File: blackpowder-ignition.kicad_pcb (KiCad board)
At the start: 2 copper layers, 63.5 x 63.5 mm, 42 parts, among them J1 CAS_stacking, J2 Conn_01x02, J3 Conn_01x02, J4 Conn_01x02, J5 Conn_01x02, J8 Conn_01x02, Q1 FDS6898A, Q2 FDS6898A, Q3 FDS6898A, Q4 FDS6898A, U1 TCA9534

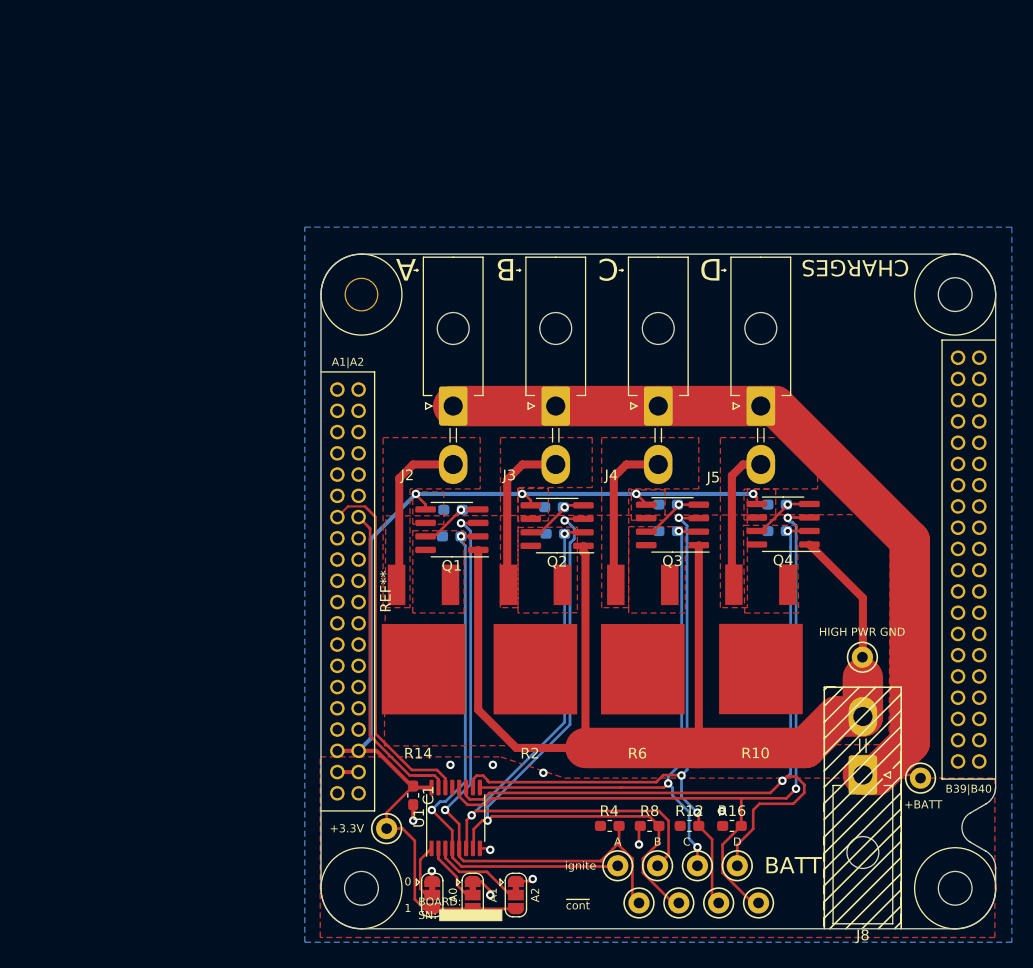
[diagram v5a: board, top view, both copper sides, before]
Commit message: 8 charges on a module
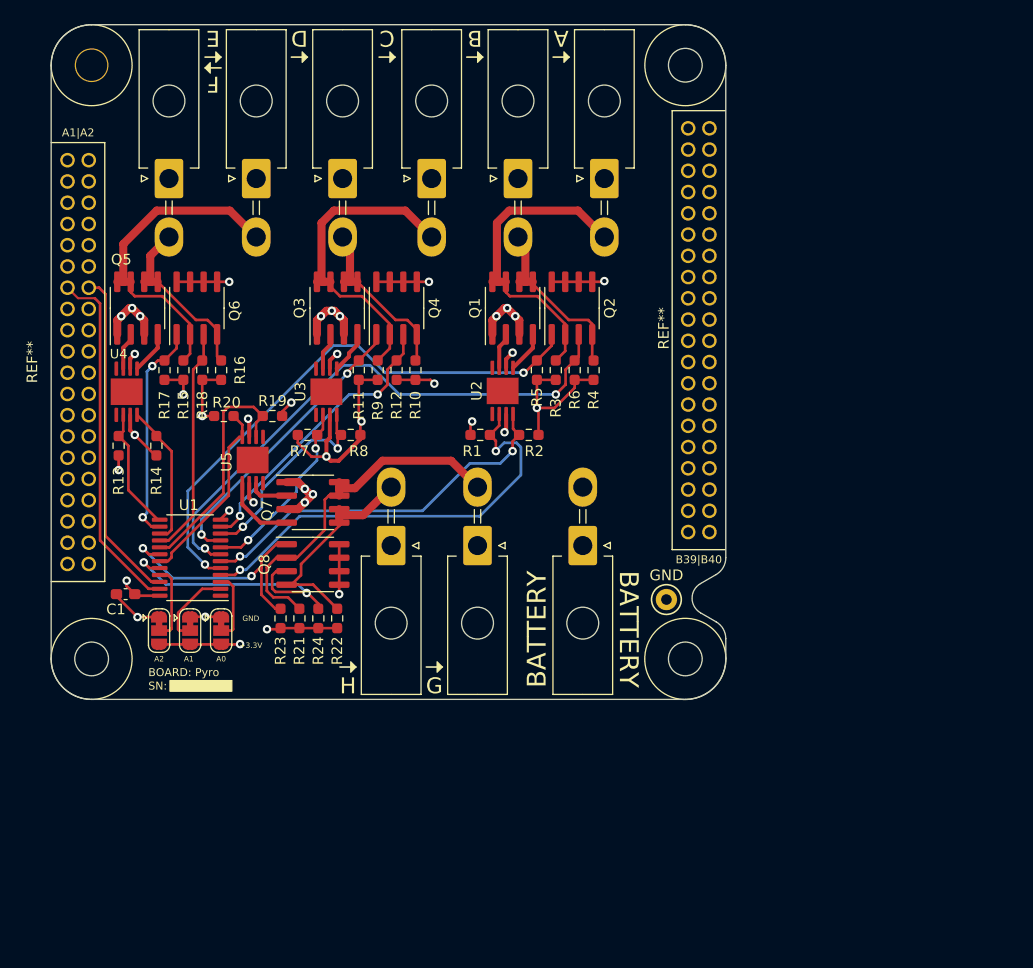
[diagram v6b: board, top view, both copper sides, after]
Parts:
- removed TP10, TP11, TP9: TestPoint, star-common-lib:TestPoint_Keystone_5000_Miniature
- removed TP2, TP3, TP4, TP5, TP6, TP7, TP8: TestPoint, star-common-lib:TestPoint_Keystone_5117_Miniature
- added J10: Conn_01x02, star-common-lib:Molex_Mini-Fit_Jr_5569-02A2_2x01_P4.20mm_Horizontal, F.Cu at (58.7, 70.6)
- added J6: Conn_01x02, star-common-lib:Molex_Mini-Fit_Jr_5569-02A2_2x01_P4.20mm_Horizontal, F.Cu at (46.0, 36.1)
- added J7: Conn_01x02, star-common-lib:Molex_Mini-Fit_Jr_5569-02A2_2x01_P4.20mm_Horizontal, F.Cu at (37.8, 36.1)
- added J9: Conn_01x02, star-common-lib:Molex_Mini-Fit_Jr_5569-02A2_2x01_P4.20mm_Horizontal, F.Cu at (66.8, 70.6)
- added Q5: FDS6898A, Package_SO:SOIC-8_3.9x4.9mm_P1.27mm, F.Cu at (34.8, 48.3)
- added Q6: FDS6898A, Package_SO:SOIC-8_3.9x4.9mm_P1.27mm, F.Cu at (40.4, 48.3)
- added Q7: FDS6898A, Package_SO:SOIC-8_3.9x4.9mm_P1.27mm, F.Cu at (51.3, 66.5)
- added Q8: FDS6898A, Package_SO:SOIC-8_3.9x4.9mm_P1.27mm, F.Cu at (51.3, 72.4)
- added R17: 50k, Resistor_SMD:R_0603_1608Metric_Pad0.98x0.95mm_HandSolder, F.Cu at (37.3, 54.1)
- added R18: 50k, Resistor_SMD:R_0603_1608Metric_Pad0.98x0.95mm_HandSolder, F.Cu at (40.9, 54.1)
- added R19: 100k, Resistor_SMD:R_0603_1608Metric_Pad0.98x0.95mm_HandSolder, F.Cu at (47.5, 58.4)
- added R20: 100k, Resistor_SMD:R_0603_1608Metric_Pad0.98x0.95mm_HandSolder, F.Cu at (42.9, 58.4)
- added R21: 100k, Resistor_SMD:R_0603_1608Metric_Pad0.98x0.95mm_HandSolder, F.Cu at (50.0, 77.5)
- added R22: 100k, Resistor_SMD:R_0603_1608Metric_Pad0.98x0.95mm_HandSolder, F.Cu at (53.6, 77.5)
- added R23: 50k, Resistor_SMD:R_0603_1608Metric_Pad0.98x0.95mm_HandSolder, F.Cu at (48.3, 77.5)
- added R24: 50k, Resistor_SMD:R_0603_1608Metric_Pad0.98x0.95mm_HandSolder, F.Cu at (51.8, 77.5)
- added U2: TC4427AVOA, Package_SO:MSOP-8-1EP_3x3mm_P0.65mm_EP2.5x3mm_Mask1.73x2.36mm, F.Cu at (69.2, 56.1)
- added U3: TC4427AVOA, Package_SO:MSOP-8-1EP_3x3mm_P0.65mm_EP2.5x3mm_Mask1.73x2.36mm, F.Cu at (52.6, 56.1)
- added U4: TC4427AVOA, Package_SO:MSOP-8-1EP_3x3mm_P0.65mm_EP2.5x3mm_Mask1.73x2.36mm, F.Cu at (33.8, 56.1)
- added U5: TC4427AVOA, Package_SO:MSOP-8-1EP_3x3mm_P0.65mm_EP2.5x3mm_Mask1.73x2.36mm, F.Cu at (45.6, 62.6)
- C1: footprint Capacitor_SMD:C_0603_1608Metric_Pad1.05x0.95mm_HandSolder -> Capacitor_SMD:C_0603_1608Metric_Pad1.08x0.95mm_HandSolder
- R1, R13, R15, R3, R7, R9: footprint Resistor_SMD:R_0603_1608Metric_Pad1.05x0.95mm_HandSolder -> Resistor_SMD:R_0603_1608Metric_Pad0.98x0.95mm_HandSolder; moved to F.Cu
- R10, R14, R2: value 3R -> 100k; footprint star-common-lib:PWR163 -> Resistor_SMD:R_0603_1608Metric_Pad0.98x0.95mm_HandSolder
- R11, R5: value 100k -> 50k; footprint Resistor_SMD:R_0603_1608Metric_Pad1.05x0.95mm_HandSolder -> Resistor_SMD:R_0603_1608Metric_Pad0.98x0.95mm_HandSolder; moved to F.Cu
- R12: footprint Resistor_SMD:R_0603_1608Metric_Pad1.05x0.95mm_HandSolder -> Resistor_SMD:R_0603_1608Metric_Pad0.98x0.95mm_HandSolder
- R16, R4, R8: value 50k -> 100k; footprint Resistor_SMD:R_0603_1608Metric_Pad1.05x0.95mm_HandSolder -> Resistor_SMD:R_0603_1608Metric_Pad0.98x0.95mm_HandSolder
- R6: value 3R -> 50k; footprint star-common-lib:PWR163 -> Resistor_SMD:R_0603_1608Metric_Pad0.98x0.95mm_HandSolder
- TP1: footprint star-common-lib:TestPoint_Keystone_5117_Miniature -> TestPoint:TestPoint_Keystone_5000-5004_Miniature
- U1: value TCA9534 -> TCA9555PWR; footprint Package_SO:TSSOP-16_4.4x5mm_P0.65mm -> Package_SO:TSSOP-24_4.4x7.8mm_P0.65mm
- moved R16 64.4 mm to (42.7, 54.1), turned to 270 degrees
- moved R13 62.5 mm to (33.0, 61.2), turned to 270 degrees
- moved R15 57.3 mm to (39.1, 54.1), turned to 270 degrees
- moved R12 51.0 mm to (59.2, 54.1), turned to 270 degrees
- moved R8 46.3 mm to (54.9, 60.2), turned to 0 degrees
- moved J5 44.8 mm to (54.1, 36.1)
- moved R4 42.9 mm to (77.7, 54.1), turned to 270 degrees
- moved JP3 41.8 mm to (36.8, 78.6)
- moved Q4 41.7 mm to (59.2, 48.3), turned to 90 degrees
- moved R10 40.3 mm to (61.0, 54.1), turned to 270 degrees
- moved Q3 37.6 mm to (53.6, 48.3), turned to 90 degrees
- moved JP2 36.4 mm to (39.8, 78.6)
- moved U1 35.0 mm to (39.8, 71.8), turned to 180 degrees
- moved J8 34.1 mm to (76.7, 70.6)
- moved J1 33.3 mm to (26.7, 21.6)
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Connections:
- J1 pad A26: Net-(J1-PadA26) -> GND
- J1 pad A30: Net-(J1-PadA30) -> GND
- J1 pad A34: Net-(J1-PadA34) -> GND
- J1 pad A5: Net-(J1-PadA5) -> +5V
- J1 pad A6: Net-(J1-PadA6) -> +5V
- Q1 pad 2: /igniteA -> Net-(Q1-Pad2)
- Q1 pad 3: /~contA~ -> GND
- Q1 pad 5: +3V3 -> Net-(J3-Pad2)
- Q1 pad 6: +3V3 -> Net-(J3-Pad2)
- Q1 pad 7: Net-(Q1-Pad4) -> Net-(J2-Pad2)
- Q1 pad 8: Net-(Q1-Pad4) -> Net-(J2-Pad2)
- Q2 pad 1: GND -> /contA
- Q2 pad 2: /igniteB -> Net-(J2-Pad2)
- Q2 pad 3: /~contB~ -> /contB
- Q2 pad 4: Net-(Q2-Pad4) -> Net-(J3-Pad2)
- Q2 pad 7: Net-(Q2-Pad4) -> +3V3
- Q2 pad 8: Net-(Q2-Pad4) -> +3V3
- Q3 pad 2: /igniteC -> Net-(Q3-Pad2)
- Q3 pad 3: /~contC~ -> GND
- Q3 pad 5: +3V3 -> Net-(J5-Pad2)
- Q3 pad 6: +3V3 -> Net-(J5-Pad2)
- Q3 pad 7: Net-(Q3-Pad4) -> Net-(J4-Pad2)
- Q3 pad 8: Net-(Q3-Pad4) -> Net-(J4-Pad2)
- Q4 pad 1: GND -> /contC
- Q4 pad 2: /igniteD -> Net-(J4-Pad2)
- Q4 pad 3: /~contD~ -> /contD
- Q4 pad 4: Net-(Q4-Pad4) -> Net-(J5-Pad2)
- Q4 pad 7: Net-(Q4-Pad4) -> +3V3
- Q4 pad 8: Net-(Q4-Pad4) -> +3V3
- R10 pad 2: Net-(Q4-Pad4) -> GND
- R11 pad 1: Net-(Q3-Pad4) -> /contC
- R12 pad 1: /~contC~ -> /contD
- R13 pad 1: /igniteD -> /igniteE
- R14 pad 1: Net-(J2-Pad2) -> /igniteF
- R14 pad 2: Net-(Q1-Pad4) -> GND
- R15 pad 1: Net-(Q4-Pad4) -> Net-(J6-Pad2)
- R16 pad 1: /~contD~ -> Net-(J7-Pad2)
- R2 pad 1: Net-(J3-Pad2) -> /igniteB
- R2 pad 2: Net-(Q2-Pad4) -> GND
- R3 pad 1: Net-(Q1-Pad4) -> Net-(J2-Pad2)
- R4 pad 1: /~contA~ -> Net-(J3-Pad2)
- R5 pad 1: /igniteB -> /contA
- R6 pad 1: Net-(J4-Pad2) -> /contB
- R6 pad 2: Net-(Q3-Pad4) -> GND
- R7 pad 1: Net-(Q2-Pad4) -> /igniteC
- R8 pad 1: /~contB~ -> /igniteD
- R9 pad 1: /igniteC -> Net-(J4-Pad2)
- TP1 pad 1: /igniteA -> GND
- U1 pad 1: /A0 -> Net-(U1-Pad1)
- U1 pad 10: /~contC~ -> /igniteD
- U1 pad 11: /igniteD -> /contD
- U1 pad 12: /~contD~ -> GND
- U1 pad 13: Net-(U1-Pad13) -> /igniteE
- U1 pad 14: /SCL -> /contE
- U1 pad 15: /SDA -> /igniteF
- U1 pad 16: +3V3 -> /contF
- U1 pad 3: /A2 -> /A0
- U1 pad 5: /~contA~ -> /contA
- U1 pad 7: /~contB~ -> /contB
- U1 pad 8: GND -> /igniteC
- U1 pad 9: /igniteC -> /contC
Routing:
- net +3V3: track 98.0 -> 206.5 mm, vias 4 -> 6
- net +5V: track 0.00 -> 79.9 mm, vias 0 -> 4
- net +BATT: track 78.1 -> 0.00 mm
- net /~contD~: track 73.8 -> 0.00 mm, vias 2 -> 0
- net /~contB~: track 63.7 -> 0.00 mm, vias 2 -> 0
- net /~contC~: track 61.3 -> 0.00 mm, vias 3 -> 0
- net /~contA~: track 59.0 -> 0.00 mm, vias 2 -> 0
- net /contB: track 0.00 -> 53.3 mm, vias 0 -> 2
- net /igniteD: track 72.0 -> 19.2 mm
- net /contA: track 0.00 -> 52.3 mm, vias 0 -> 2
- net /igniteC: track 53.1 -> 17.6 mm, vias 3 -> 2
- net Net-(J9-Pad2): track 0.00 -> 33.7 mm
- net Net-(J6-Pad2): track 0.00 -> 31.2 mm
- net /contC: track 0.00 -> 27.7 mm, vias 0 -> 2
- net /contD: track 0.00 -> 27.5 mm, vias 0 -> 2
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- added copper zone on In2.Cu, net +BATT
- added copper zone on In1.Cu, net GND
- removed copper zone on F.Cu, net +3V3
- removed copper zone on B.Cu, net GND
- removed copper zone on F.Cu, net GND
- removed copper zone on F.Cu, net Net-(J2-Pad2)
- removed copper zone on F.Cu, net Net-(J3-Pad2)
- removed copper zone on F.Cu, net Net-(J4-Pad2)
- removed copper zone on F.Cu, net Net-(J5-Pad2)
- removed copper zone on F.Cu, net Net-(Q1-Pad4)
- removed copper zone on F.Cu, net Net-(Q2-Pad4)
- removed copper zone on F.Cu, net Net-(Q3-Pad4)
- removed copper zone on F.Cu, net Net-(Q4-Pad4)
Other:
- copper layers 2 -> 4
- net class BusFanOut added: clearance 0.2032, trace_width 0.2032, via_dia 0.8, via_drill 0.4
- board text added: "BATTERY"
- board text added: "E"
- board text added: "F"
- board text added: "G"
- board text added: "GND"
- board text added: "H"
- board text removed: "+BATT"
- board text removed: "0"
- board text removed: "1"
- board text removed: "BATT"
- board text removed: "CHARGES"
- board text removed: "HIGH PWR GND"
- board text removed: "ignite"
- board text removed: "~cont~"

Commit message: addressed review comments
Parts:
- added G***: LOGO, star-common-lib:star_6x5_2, F.Cu at (50.3, 81.5)
- JP1, JP2, JP3: value SolderJumper_3_Bridged12 -> SolderJumper_3; footprint Jumper:SolderJumper-3_P1.3mm_Bridged12_RoundedPad1.0x1.5mm -> Jumper:SolderJumper-3_P1.3mm_Open_RoundedPad1.0x1.5mm
- Q2, Q4, Q6, Q8: value FDS6898A -> Q_DUAL_PMOS_S1G1D2S2G2D1; footprint Package_SO:SOIC-8_3.9x4.9mm_P1.27mm -> Package_TO_SOT_SMD:SOT-363_SC-70-6_Handsoldering
- moved R17 12.1 mm to (49.3, 52.3)
- moved R18 10.3 mm to (51.1, 52.3)
- moved R5 10.2 mm to (82.3, 51.8)
- moved R11 10.1 mm to (65.5, 51.9)
- moved R14 9.25 mm to (45.5, 58.7), turned to 0 degrees
- moved R12 8.47 mm to (67.4, 51.9)
- moved R6 8.44 mm to (84.1, 51.8)
- moved J3 8.38 mm to (79.0, 36.1)
- moved J4 8.38 mm to (54.1, 36.1)
- moved J5 8.38 mm to (62.5, 36.1)
- moved J7 8.21 mm to (46.0, 36.1)
- moved J2 8.13 mm to (70.6, 36.1)
- moved J6 8.13 mm to (37.8, 36.1)
- moved U4 8.05 mm to (41.8, 56.3)
- moved R20 7.95 mm to (39.4, 65.5), turned to 90 degrees
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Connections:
- Q2 pad 1: /contA -> /~contB~
- Q2 pad 3: /contB -> +3V3
- Q2 pad 4: Net-(J3-Pad2) -> /~contA~
- Q2 pad 5: +3V3 -> Net-(J3-Pad2)
- Q4 pad 1: /contC -> /~contD~
- Q4 pad 3: /contD -> +3V3
- Q4 pad 4: Net-(J5-Pad2) -> /~contC~
- Q4 pad 5: +3V3 -> Net-(J5-Pad2)
- Q6 pad 1: /contE -> /~contF~
- Q6 pad 3: /contF -> +3V3
- Q6 pad 4: Net-(J7-Pad2) -> /~contE~
- Q6 pad 5: +3V3 -> Net-(J7-Pad2)
- Q8 pad 1: /contG -> /~contH~
- Q8 pad 3: /contH -> +3V3
- Q8 pad 4: Net-(J10-Pad2) -> /~contG~
- Q8 pad 5: +3V3 -> Net-(J10-Pad2)
- R1 pad 1: /igniteA -> /igniteB
- R11 pad 1: /contC -> /~contD~
- R12 pad 1: /contD -> /~contC~
- R13 pad 1: /igniteE -> /igniteF
- R14 pad 1: /igniteF -> /igniteE
- R17 pad 1: /contE -> /~contF~
- R18 pad 1: /contF -> /~contE~
- R19 pad 1: /igniteG -> /igniteH
- R2 pad 1: /igniteB -> /igniteA
- R20 pad 1: /igniteH -> /igniteG
- R23 pad 1: /contG -> /~contH~
- R24 pad 1: /contH -> /~contG~
- R5 pad 1: /contA -> /~contB~
- R6 pad 1: /contB -> /~contA~
- R7 pad 1: /igniteC -> /igniteD
- R8 pad 1: /igniteD -> /igniteC
- U1 pad 11: /contD -> /~contD~
- U1 pad 14: /contE -> /~contE~
- U1 pad 16: /contF -> /~contF~
- U1 pad 18: /contG -> /~contG~
- U1 pad 20: /contH -> /~contH~
- U1 pad 5: /contA -> /~contA~
- U1 pad 7: /contB -> /~contB~
- U1 pad 9: /contC -> /~contC~
- U2 pad 2: /igniteA -> /igniteB
- U2 pad 4: /igniteB -> /igniteA
- U3 pad 2: /igniteC -> /igniteD
- U3 pad 4: /igniteD -> /igniteC
- U4 pad 2: /igniteE -> /igniteF
- U4 pad 4: /igniteF -> /igniteE
- U5 pad 2: /igniteG -> /igniteH
- U5 pad 4: /igniteH -> /igniteG
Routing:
- net +3V3: track 206.5 -> 22.2 mm, vias 6 -> 10
- net /~contA~: track 0.00 -> 58.2 mm, vias 0 -> 2
- net /~contB~: track 0.00 -> 56.8 mm, vias 0 -> 2
- net /contB: track 53.3 -> 0.00 mm, vias 2 -> 0
- net /contA: track 52.3 -> 0.00 mm, vias 2 -> 0
- net GND: track 140.4 -> 93.6 mm, vias 28 -> 41
- net /~contF~: track 0.00 -> 41.2 mm, vias 0 -> 2
- net /~contD~: track 0.00 -> 39.5 mm, vias 0 -> 2
- net /~contC~: track 0.00 -> 38.1 mm, vias 0 -> 2
- net /~contE~: track 0.00 -> 33.6 mm, vias 0 -> 2
- net /contC: track 27.7 -> 0.00 mm, vias 2 -> 0
- net /contD: track 27.5 -> 0.00 mm, vias 2 -> 0
- net /~contG~: track 0.00 -> 26.9 mm, vias 0 -> 2
- net /contH: track 26.4 -> 0.00 mm, vias 2 -> 0
- net /contG: track 23.2 -> 0.00 mm, vias 2 -> 0
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- added copper zone on B.Cu, net +3V3
- added copper zone on F.Cu, net GND
- added copper zone on F.Cu, net Net-(J10-Pad2)
- added copper zone on F.Cu, net Net-(J2-Pad2)
- added copper zone on F.Cu, net Net-(J3-Pad2)
- added copper zone on F.Cu, net Net-(J4-Pad2)
- added copper zone on F.Cu, net Net-(J5-Pad2)
- added copper zone on F.Cu, net Net-(J6-Pad2)
- added copper zone on F.Cu, net Net-(J7-Pad2)
- added copper zone on F.Cu, net Net-(J9-Pad2)
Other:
- net class Default: clearance 0.254 -> 0.2032
- rule trace_clearance: 0.254 -> 0.2032

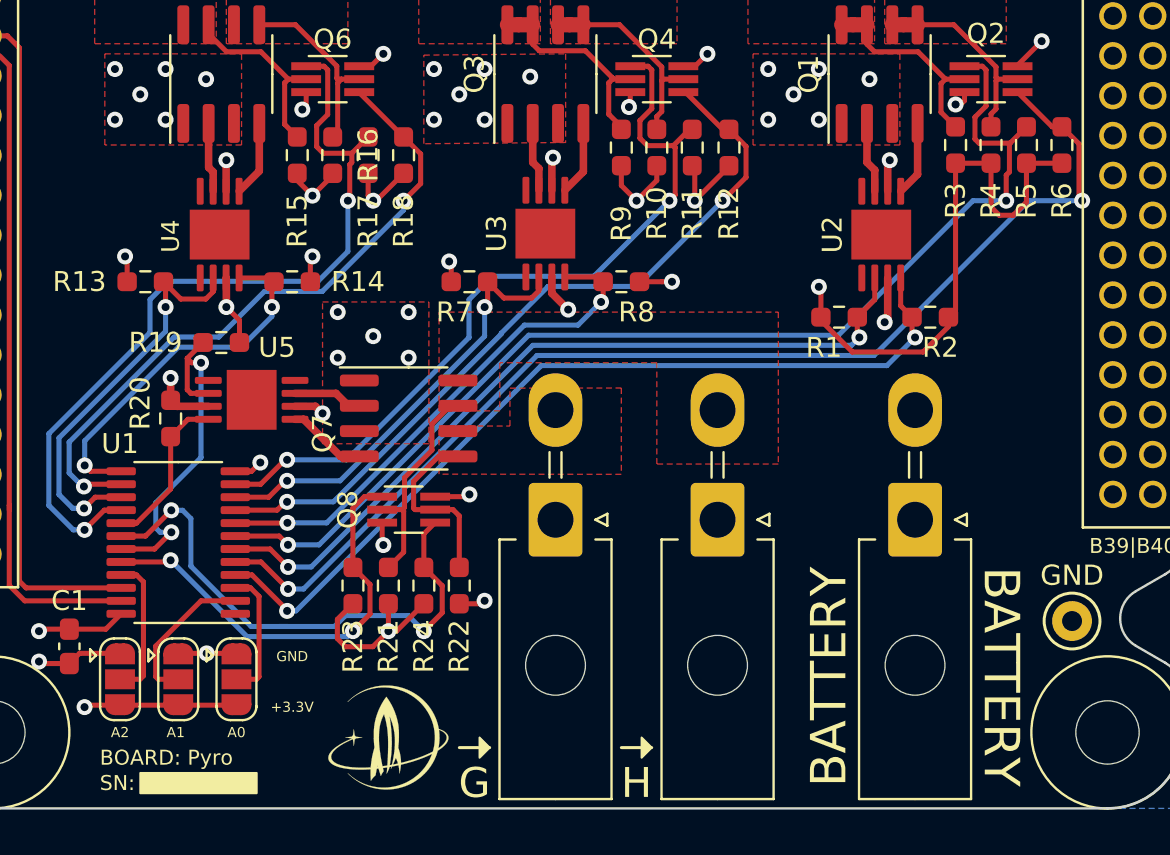
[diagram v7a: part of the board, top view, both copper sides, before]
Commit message: added digikey and manf part numbers, BAC logo
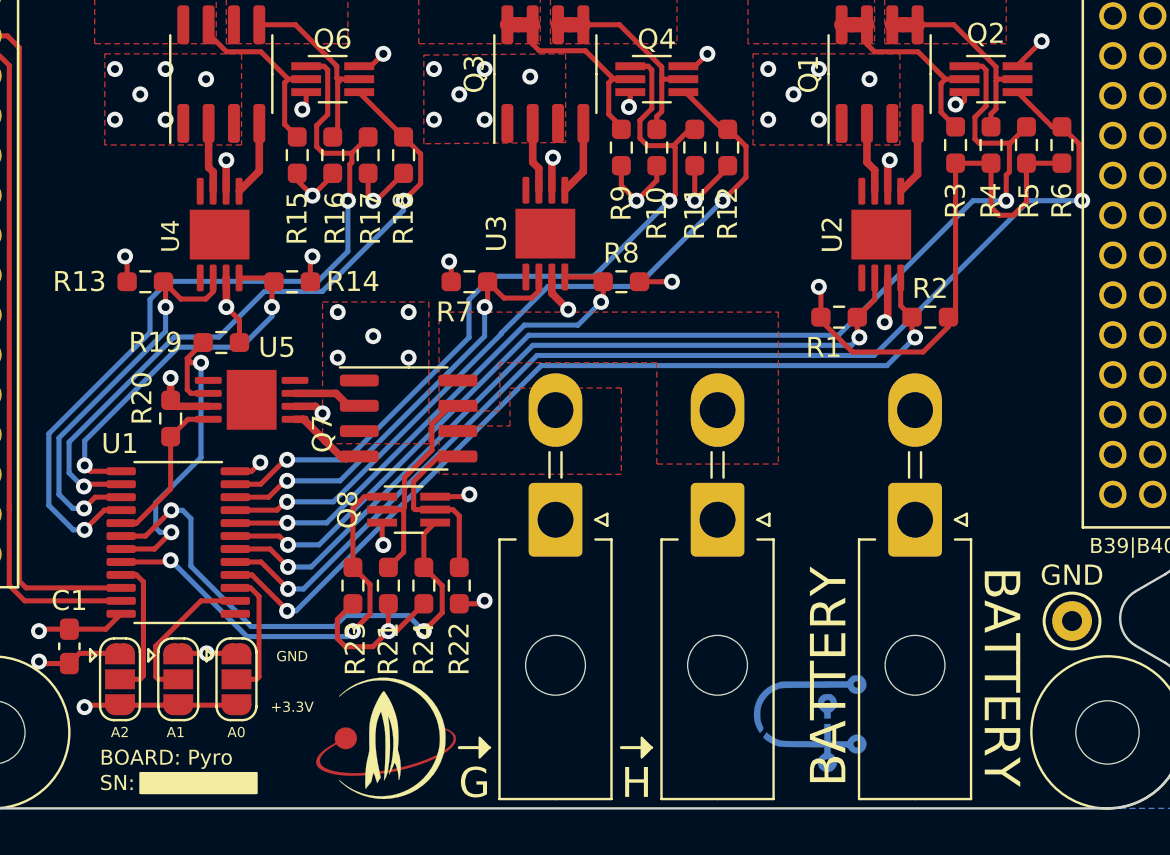
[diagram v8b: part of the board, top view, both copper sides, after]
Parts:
- removed G***: LOGO, star-common-lib:star_6x5_2
- added Ref**: Val**, star-common-lib:star_fancy, F.Cu at (50.2, 81.5)
- added Ref**: Val**, star-common-lib:bac, B.Cu at (71.4, 81.3)
- R1, R10, R13, R14, R15, R16, R19, R2, R20, R21, R22, R3, R4, R7, R8, R9: value 100k -> 50k
- moved R11 0.13 mm to (65.7, 51.9)
- moved R12 0.06 mm to (67.3, 51.9)
